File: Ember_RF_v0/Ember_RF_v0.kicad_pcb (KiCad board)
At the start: 4 copper layers, 98.2 x 84.5 mm, 8 parts

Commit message: All routings completed, Lisan Al-gaib!
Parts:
- removed X1: ~, adafruit:SMA90_DIP
- added ?: , rx_label:RX0, F.Cu at (142.1, 116.5)
- added ?: , 7v4_label:7V40, F.Cu at (142.1, 124.1)
- added ?: , gnd_label:GND0, F.Cu at (142.1, 121.6)
- added ?: , tx_label:TX0, F.Cu at (142.1, 119.0)
- added C5: 10 uF, microbuilder:0603, B.Cu at (183.6, 109.2)
- added C6: 10 uF, microbuilder:0603, B.Cu at (177.4, 120.8)
- added C7: 10 uF, microbuilder:0603, B.Cu at (177.4, 122.7)
- added G***: LOGO, RT_Graphics:RT_logo, F.Cu at (155.0, 120.0)
- added G***: LOGO, RT_Graphics:TDU_label, F.Cu at (181.3, 46.1)
- added G***: LOGO, RT_Graphics:Ember_logo, F.Cu at (167.5, 119.5)
- added J1: ~, sma-connector:RFSOLUTIONS_CON-SMA-EDGE-S, F.Cu at (162.0, 42.2)
- added LED1: BATT_CONN, microbuilder:CHIPLED_0603, F.Cu at (181.8, 107.2)
- added LS2: BUZZER, CMT-8530S-SMT:CUI_CMT-8530S-SMT, B.Cu at (180.9, 98.4)
- added Q5: CJ3400, CJ3400:SOT95P240X115-3N, B.Cu at (182.3, 90.7)
- added R15: 100, microbuilder:0603, B.Cu at (183.7, 105.2)
- added R17: 100, microbuilder:0603, F.Cu at (184.2, 107.2)
- added R27: 1k, microbuilder:0603, B.Cu at (176.7, 86.1)
- added R4: 33k, microbuilder:0603, B.Cu at (181.5, 86.1)
- added REF**: KiCad-Logo2_5mm_SilkScreen, Symbol:KiCad-Logo2_5mm_SilkScreen, F.Cu at (142.0, 47.4)
- added REF**: MountingHole_3.2mm_M3_DIN965_Pad_TopOnly, MountingHole:MountingHole_3.2mm_M3_DIN965_Pad_TopOnly, F.Cu at (180.5, 78.0)
- added REF**: MountingHole_3.2mm_M3_DIN965_Pad_TopOnly, MountingHole:MountingHole_3.2mm_M3_DIN965_Pad_TopOnly, F.Cu at (142.5, 58.0)
- added REF**: MountingHole_3.2mm_M3_DIN965_Pad_TopOnly, MountingHole:MountingHole_3.2mm_M3_DIN965_Pad_TopOnly, F.Cu at (142.5, 78.0)
- added REF**: MountingHole_3.2mm_M3_DIN965_Pad_TopOnly, MountingHole:MountingHole_3.2mm_M3_DIN965_Pad_TopOnly, F.Cu at (180.5, 58.0)
- added U4: LDO Regulator 5v, AMS1117-5.0:SOT229P700X180-4N, B.Cu at (181.8, 114.5)
- U1: moved to B.Cu
- U2, U3: moved to F.Cu
- moved U3 82.1 mm to (162.3, 67.2), turned to 180 degrees
- moved JP2 80.9 mm to (139.9, 120.3), turned to 90 degrees
- moved U2 79.6 mm to (153.7, 101.5), turned to 90 degrees
- moved R1 76.7 mm to (177.0, 65.2), turned to -90 degrees
- moved R3 73.9 mm to (176.9, 99.1), turned to 90 degrees
- moved R2 73.1 mm to (176.9, 95.3), turned to 90 degrees
- moved U1 43.0 mm to (162.0, 102.6)
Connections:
- JP2 pad 1: /5V -> /V_BATT
- U1 pad P$24: unconnected-(U1-GP18-PadP$24) -> /BUZZER
- U1 pad P$39: /5V -> /5v
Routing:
- net /3v3: track 9.96 -> 167.6 mm, vias 3 -> 1
- net /GND: track 73.5 -> 0.00 mm, vias 4 -> 18
- net /GPS_WAKE_UP: track 100.4 -> 29.6 mm
- net /V_BATT: track 0.00 -> 68.7 mm, vias 0 -> 1
- net /GPS_RESET: track 85.4 -> 25.8 mm
- net /5v: track 0.00 -> 39.7 mm
- net /GPS_TX: track 39.3 -> 4.94 mm
- net /GPS_RX: track 35.4 -> 13.2 mm
- net /LORA_DIO1: track 31.3 -> 51.7 mm
- net /SCL: track 61.9 -> 41.7 mm
- net /5V: track 20.0 -> 0.00 mm
- net /LORA_CS: track 60.1 -> 44.3 mm
- net /LORA_SCK: track 49.6 -> 36.8 mm
- net /LORA_MISO: track 52.9 -> 40.3 mm
- net Net-(U3-ANT): track 8.52 -> 20.2 mm
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- added copper zone on B.Cu, net /GND
- added copper zone on F.Cu, net /GND
- removed copper zone on In1.Cu, net /3v3
- removed copper zone on In2.Cu, net /GND
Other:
- board size 98.2 x 84.5 mm -> 54 x 90.6 mm
- copper layers 4 -> 2
- board text added: "EMBER V0.2"

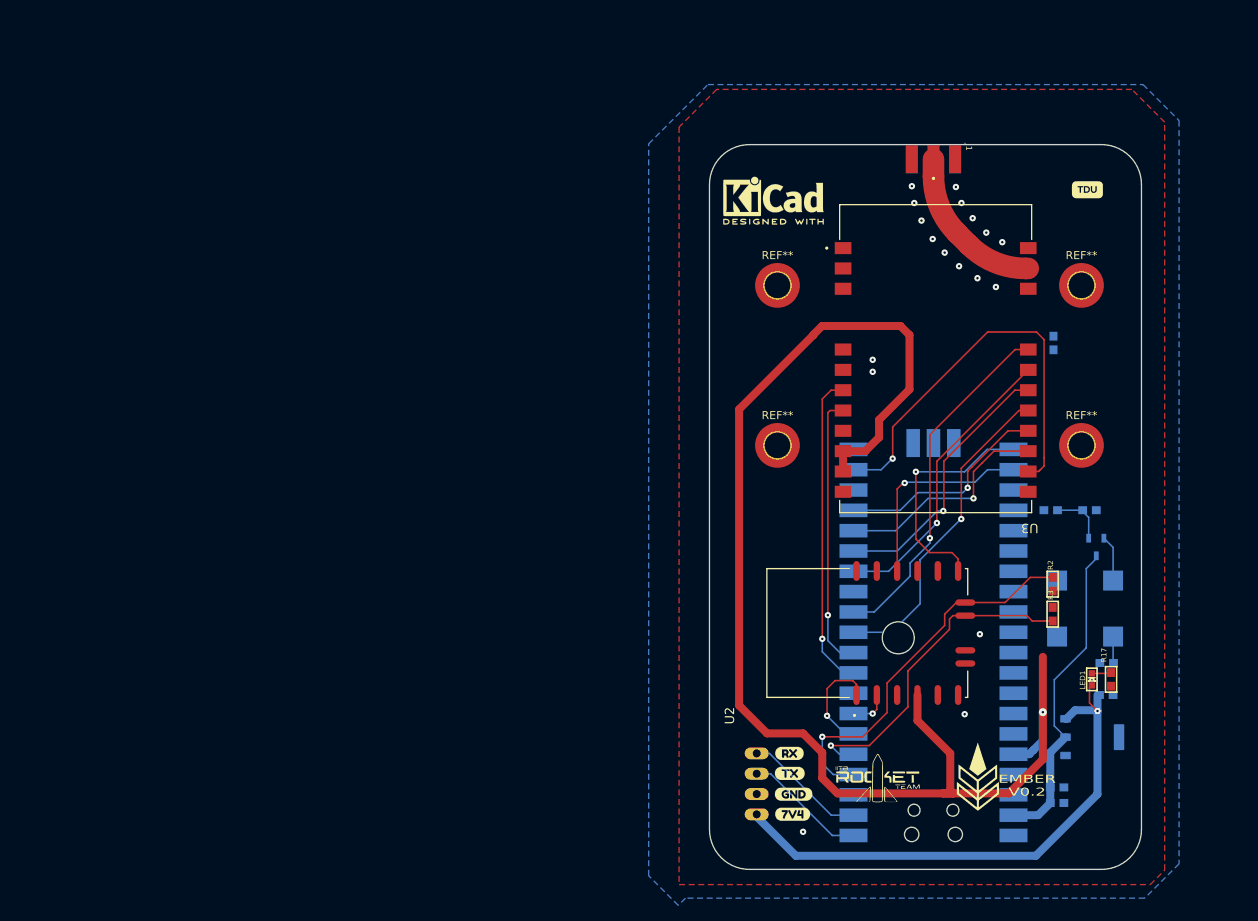
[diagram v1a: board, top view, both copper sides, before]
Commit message: TDU board LDO is replaced by AP63205
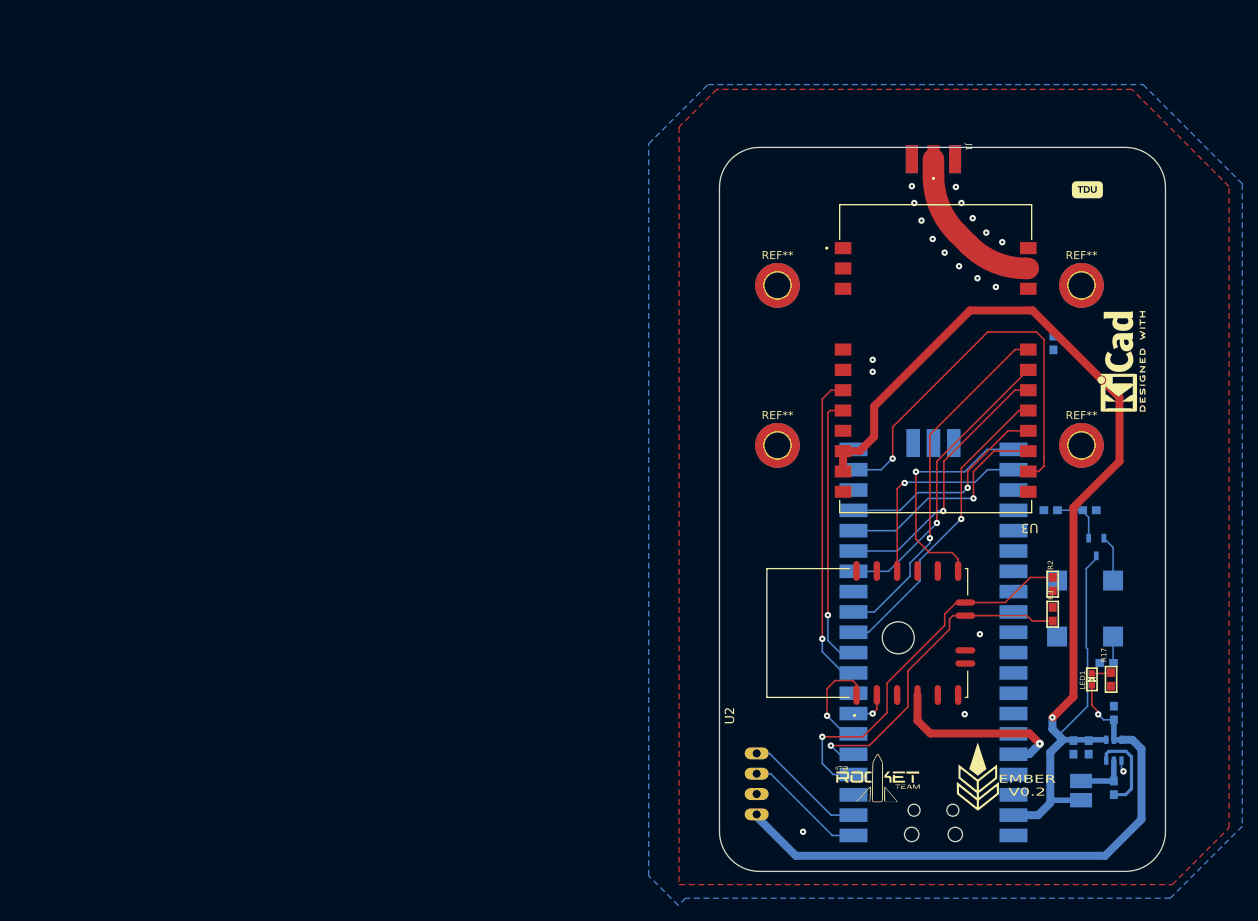
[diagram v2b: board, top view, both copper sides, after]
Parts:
- removed ?: , rx_label:RX0
- removed ?: , 7v4_label:7V40
- removed ?: , gnd_label:GND0
- removed ?: , tx_label:TX0
- removed C5, C6, C7: 10 uF, microbuilder:0603
- removed the REF** at (180.5, 78.0)
- removed the REF** at (142.5, 58.0)
- removed the REF** at (142.5, 78.0)
- removed the REF** at (180.5, 58.0)
- removed U4: LDO Regulator 5v, AMS1117-5.0:SOT229P700X180-4N
- added C1: 100nF, microbuilder:0603, B.Cu at (184.6, 120.8)
- added C2: 22uF, microbuilder:0603, B.Cu at (181.4, 115.8)
- added C3: 22uF, microbuilder:0603, B.Cu at (179.5, 115.8)
- added C4: 10uF, microbuilder:0603, B.Cu at (184.6, 111.5)
- added IC1: ~, AP63205WU-7:SOT95P280X100-6N, B.Cu at (184.6, 116.1)
- added L1: 4.7uH, SRN3015-4R7M:INDPM3027X150N, B.Cu at (180.4, 121.2)
- added REF**: MountingHole_3.2mm_M3_DIN965_Pad_TopBottom, MountingHole:MountingHole_3.2mm_M3_DIN965_Pad_TopBottom, F.Cu at (180.5, 78.0)
- added REF**: MountingHole_3.2mm_M3_DIN965_Pad_TopBottom, MountingHole:MountingHole_3.2mm_M3_DIN965_Pad_TopBottom, F.Cu at (180.5, 58.0)
- added REF**: MountingHole_3.2mm_M3_DIN965_Pad_TopBottom, MountingHole:MountingHole_3.2mm_M3_DIN965_Pad_TopBottom, F.Cu at (142.5, 58.0)
- added REF**: MountingHole_3.2mm_M3_DIN965_Pad_TopBottom, MountingHole:MountingHole_3.2mm_M3_DIN965_Pad_TopBottom, F.Cu at (142.5, 78.0)
- R1, R2, R3: value ~ -> 10k
- moved REF** 47.9 mm to (185.5, 67.5), turned to 90 degrees
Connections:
- U3 pad 10: /3v3 -> /5v
- U3 pad 9: /3v3 -> /5v
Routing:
- net /3v3: track 167.6 -> 23.5 mm
- net /5v: track 39.7 -> 146.4 mm, vias 0 -> 1
- net Net-(C1-P$1): track 0.00 -> 10.9 mm
- net Net-(C1-P$2): track 0.00 -> 6.65 mm
- net /V_BATT: track 68.7 -> 73.7 mm
- net /LORA_MISO: track 40.3 -> 38.6 mm
- net /GND: track 0.00 -> 1.45 mm, vias 18 -> 19
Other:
- board size 54 x 90.6 mm -> 55.8 x 90.5 mm

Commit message: All changes and things are done in both FCU and TDU - Lisan Al-gaib!
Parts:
- added ?: , 5v_label:5V0, F.Cu at (140.7, 70.2)
- added ?: , 7v4_label:7V40, F.Cu at (142.3, 124.2)
- added ?: , rx_label:RX0, F.Cu at (142.2, 116.5)
- added ?: , tx_label:TX0, F.Cu at (142.3, 119.1)
- added ?: , gnd_label:GND0, F.Cu at (142.3, 121.6)
- added C5: 100nF, microbuilder:0603, F.Cu at (181.2, 64.9)
- added G***: LOGO, RT_Graphics:RTN_label, F.Cu at (142.4, 67.7)
- added G***: LOGO, RT_Graphics:iitb_logo, F.Cu at (182.8, 124.4)
- added G***: LOGO, RT_Graphics:CAM_PWR_label, F.Cu at (141.1, 64.7)
- added G***: LOGO, RT_Graphics:RT_logo_hi_res, B.Cu at (162.1, 62.4)
- added JP1: ~, microbuilder:1X02_OVAL, B.Cu at (138.7, 68.9)
- added Q2: SISA96DN-T1, SISA96DN-T1-GE3:SIS862DNT1GE3, B.Cu at (145.1, 69.0)
- added R30: 33k, microbuilder:0603, B.Cu at (144.3, 65.4)
- added R31: 1k, microbuilder:0603, B.Cu at (144.3, 63.5)
- moved G*** 18.8 mm to (173.2, 124.8)
- moved G*** 15.4 mm to (152.3, 121.9)
- moved REF** 4.06 mm to (183.0, 70.7), turned to 0 degrees
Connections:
- U1 pad P$20: unconnected-(U1-GP15-PadP$20) -> /CAM
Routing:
- net /5v: track 146.4 -> 183.1 mm
- net /CAM: track 0.00 -> 19.3 mm
- net /CAM_GND: track 0.00 -> 11.7 mm
- net /G_DROGUE: track 0.00 -> 4.53 mm
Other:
- board text added: "March 2026"

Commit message: v0.2 and RF v0 sent for fab - Lisan Al-gaib
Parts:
- added C6: 100nF, microbuilder:0603, F.Cu at (160.8, 112.0)
- added C7: 100nF, microbuilder:0603, F.Cu at (147.4, 82.1)
- added D1: RSX501LAM20TR, RSX501LAM20TR:DIOM4725X105N, B.Cu at (184.7, 126.3)
- C5: value 100nF -> 10uF
- R1: moved to F.Cu
- moved C5 36.1 mm to (147.4, 77.8), turned to -90 degrees
- moved REF** 4.74 mm to (186.3, 67.3), turned to 90 degrees
- moved R1 1.71 mm to (176.8, 66.9), turned to 90 degrees
- moved G*** 0.97 mm to (183.8, 124.6)
- moved ? 0.11 mm to (142.2, 124.1)
- moved ? 0.07 mm to (142.2, 119.0)
- moved ? 0.07 mm to (142.2, 121.5)
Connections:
- C4 pad 1: /V_BATT -> Net-(C4-P$1)
- IC1 pad 2: /V_BATT -> Net-(C4-P$1)
- IC1 pad 3: /V_BATT -> Net-(C4-P$1)
- REF** pad 1: (no net) -> /GND (x4)
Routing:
- net Net-(C4-P$1): track 0.00 -> 17.1 mm
- net /TXEN: track 34.3 -> 47.7 mm
- net /RXEN: track 39.6 -> 52.5 mm
- net /5v: track 183.1 -> 190.8 mm
- net /V_BATT: track 73.7 -> 67.1 mm
- net /3v3: track 23.5 -> 17.2 mm
- net /LORA_DIO1: track 51.7 -> 56.2 mm
- net /LORA_CS: track 44.3 -> 47.3 mm
- net /SCL: track 41.7 -> 42.8 mm
- net /GND: vias 19 -> 29
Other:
- board text added: "Just add MOAR power - The same wise man"
- board text added: "Switching Converter Lessgooo!"
- board text added: "Tumlogon ka antenna itna lamba kyu h? - Self explanatory"
- board text added: "{dblquote}No, hear me out now You're gonna listen to me, like it or not Right now, hear me out now You're gonna listen to me, like it or not{dblquote} - LoRa screaming at 30dBm"
